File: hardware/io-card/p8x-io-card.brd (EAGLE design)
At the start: 160 x 100 mm, 36 parts, among them J1 DIN41612-96M, J2 SERIAL, SW1 INPUT, U1 IO PAGE, U10 LED PORT, U11 MON A-LO, U12 MON A-HI, U13 MON D, U14 ACIA, U15 74HCT00, U2 PORT DEC, U3 DOE DEC, U4 DLD DEC, U5 74HCT32, U6 74HCT08, U7 BAUD DIV, U8 RS232, U9 SW IN, X2 2.4576MHZ

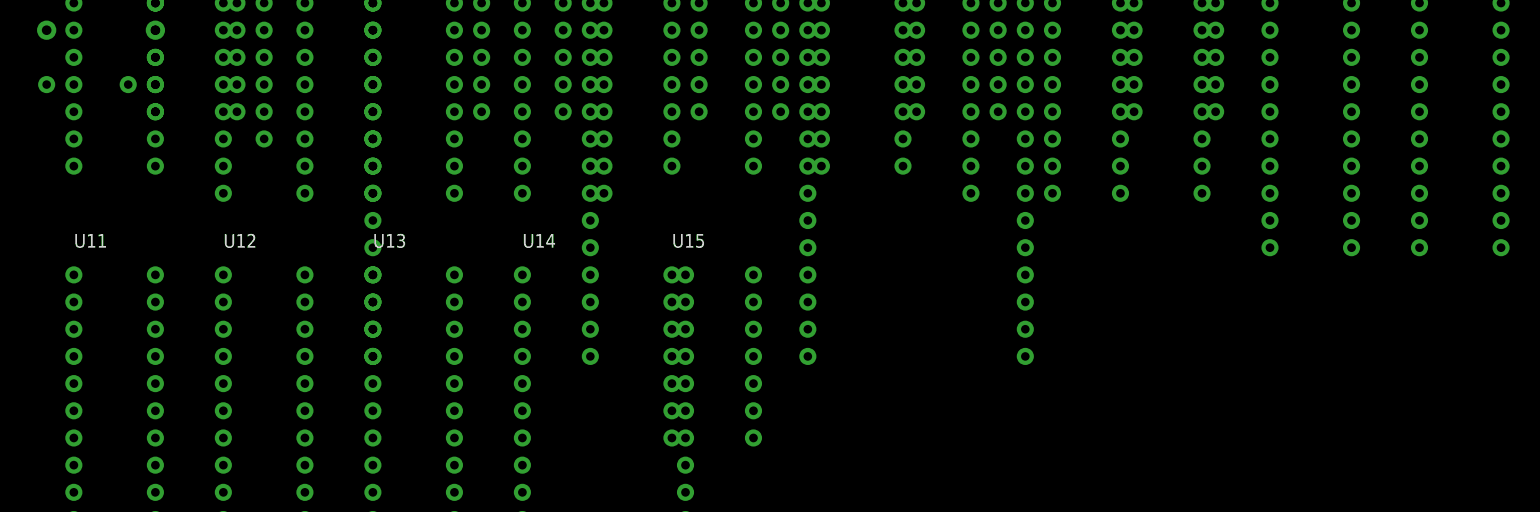
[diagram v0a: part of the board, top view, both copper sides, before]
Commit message: hw: per-IC 100nF decoupling caps on every card
card standards sec.5 requires a decoupling cap per IC; only the backplane had
them. gen_eagle's card() now generates one 100nF cap (CDn, C_DISC footprint)
per IC on the five plug-in cards, placed next to its IC and wired VCC<->GND;
the memory card's separate build does the same for U1-U9.

Caps added: control 18, regbank 44, alu 31, io 15, cf 8, memory 9. All 7
boards regenerate with 0 validation errors; card schematic PDFs refreshed.
Placement is approximate (caps sit just below each IC) pending Fusion routing.

Clears a pre-fab blocker from the backlog.

Co-Authored-By: Claude Opus 4.8 <noreply@anthropic.com>
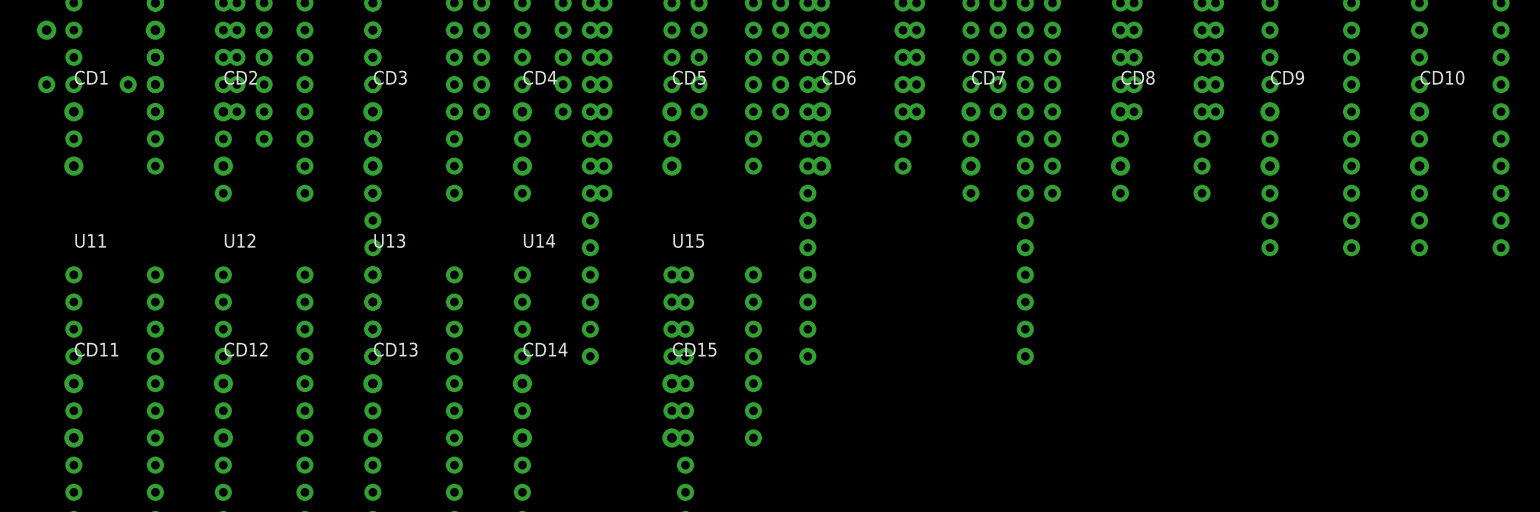
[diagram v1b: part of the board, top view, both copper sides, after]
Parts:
- added CD1, CD10, CD11, CD12, CD13, CD14, CD15, CD2, CD3, CD4, CD5, CD6, CD7, CD8, CD9: 100N, p8x:C_DISC
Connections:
- net GND: now also CD1.2, CD10.2, CD11.2, CD12.2, CD13.2, CD14.2, CD15.2, CD2.2, CD3.2, CD4.2, CD5.2, CD6.2, CD7.2, CD8.2, CD9.2
- net VCC: now also CD1.1, CD10.1, CD11.1, CD12.1, CD13.1, CD14.1, CD15.1, CD2.1, CD3.1, CD4.1, CD5.1, CD6.1, CD7.1, CD8.1, CD9.1
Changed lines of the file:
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@@
 <element name="J1" library="p8x" package="DIN96" value="DIN41612-96M" x="147.32" y="88.90"/>
 <element name="U1" library="p8x" package="DIP14" value="IO PAGE" x="7.62" y="88.90"/>
+<element name="CD1" library="p8x" package="C_DISC" value="100N" x="7.62" y="78.74"/>
 <element name="U2" library="p8x" package="DIP16" value="PORT DEC" x="21.59" y="88.90"/>
+<element name="CD2" library="p8x" package="C_DISC" value="100N" x="21.59" y="78.74"/>
 <element name="U3" library="p8x" package="DIP16" value="DOE DEC" x="35.56" y="88.90"/>
+<element name="CD3" library="p8x" package="C_DISC" value="100N" x="35.56" y="78.74"/>
 <element name="U4" library="p8x" package="DIP16" value="DLD DEC" x="49.53" y="88.90"/>
+<element name="CD4" library="p8x" package="C_DISC" value="100N" x="49.53" y="78.74"/>
 <element name="U5" library="p8x" package="DIP14" value="74HCT32" x="63.50" y="88.90"/>
+<element name="CD5" library="p8x" package="C_DISC" value="100N" x="63.50" y="78.74"/>
 <element name="U6" library="p8x" package="DIP14" value="74HCT08" x="77.47" y="88.90"/>
+<element name="CD6" library="p8x" package="C_DISC" value="100N" x="77.47" y="78.74"/>
 <element name="U7" library="p8x" package="DIP16" value="BAUD DIV" x="91.44" y="88.90"/>
+<element name="CD7" library="p8x" package="C_DISC" value="100N" x="91.44" y="78.74"/>
 <element name="U8" library="p8x" package="DIP16" value="RS232" x="105.41" y="88.90"/>
+<element name="CD8" library="p8x" package="C_DISC" value="100N" x="105.41" y="78.74"/>
 <element name="U9" library="p8x" package="DIP20" value="SW IN" x="119.38" y="88.90"/>
+<element name="CD9" library="p8x" package="C_DISC" value="100N" x="119.38" y="78.74"/>
 <element name="U10" library="p8x" package="DIP20" value="LED PORT" x="133.35" y="88.90"/>
+<element name="CD10" library="p8x" package="C_DISC" value="100N" x="133.35" y="78.74"/>
 <element name="U11" library="p8x" package="DIP20" value="MON A-LO" x="7.62" y="63.50"/>
+<element name="CD11" library="p8x" package="C_DISC" value="100N" x="7.62" y="53.34"/>
 <element name="U12" library="p8x" package="DIP20" value="MON A-HI" x="21.59" y="63.50"/>
+<element name="CD12" library="p8x" package="C_DISC" value="100N" x="21.59" y="53.34"/>
 <element name="U13" library="p8x" package="DIP20" value="MON D" x="35.56" y="63.50"/>
+<element name="CD13" library="p8x" package="C_DISC" value="100N" x="35.56" y="53.34"/>
 <element name="U14" library="p8x" package="DIP24W" value="ACIA" x="49.53" y="63.50"/>
+<element name="CD14" library="p8x" package="C_DISC" value="100N" x="49.53" y="53.34"/>
 <element name="U15" library="p8x" package="DIP14" value="74HCT00" x="63.50" y="63.50"/>
+<element name="CD15" library="p8x" package="C_DISC" value="100N" x="63.50" y="53.34"/>
 <element name="X2" library="p8x" package="OSC4" value="2.4576MHZ" x="5.08" y="96.52"/>
 <element name="SW1" library="p8x" package="DIP16" value="INPUT" x="15.24" y="96.52"/>
@@
 <contactref element="J1" pad="C31"/>
 <contactref element="J1" pad="C32"/>
+<contactref element="CD1" pad="2"/>
+<contactref element="CD2" pad="2"/>
+<contactref element="CD3" pad="2"/>
+<contactref element="CD4" pad="2"/>
+<contactref element="CD5" pad="2"/>
+<contactref element="CD6" pad="2"/>
+<contactref element="CD7" pad="2"/>
+<contactref element="CD8" pad="2"/>
+<contactref element="CD9" pad="2"/>
+<contactref element="CD10" pad="2"/>
+<contactref element="CD11" pad="2"/>
+<contactref element="CD12" pad="2"/>
+<contactref element="CD13" pad="2"/>
+<contactref element="CD14" pad="2"/>
+<contactref element="CD15" pad="2"/>
 <polygon width="0.254" layer="2" isolate="0.3" rank="1">
 <vertex x="0" y="0"/>
@@
 <contactref element="J1" pad="C1"/>
 <contactref element="J1" pad="C2"/>
+<contactref element="CD1" pad="1"/>
+<contactref element="CD2" pad="1"/>
+<contactref element="CD3" pad="1"/>
+<contactref element="CD4" pad="1"/>
+<contactref element="CD5" pad="1"/>
+<contactref element="CD6" pad="1"/>
+<contactref element="CD7" pad="1"/>
+<contactref element="CD8" pad="1"/>
+<contactref element="CD9" pad="1"/>
+<contactref element="CD10" pad="1"/>
+<contactref element="CD11" pad="1"/>
+<contactref element="CD12" pad="1"/>
+<contactref element="CD13" pad="1"/>
+<contactref element="CD14" pad="1"/>
+<contactref element="CD15" pad="1"/>
 <polygon width="0.254" layer="15" isolate="0.3" rank="1">
 <vertex x="0" y="0"/>

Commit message: feat(hw): provision RTC + CF 8-bit fallback footprints (rev C, DNP)
The last two pre-fab board items, both Do-Not-Populate so the options exist
post-fab without a respin.

- I/O card: DS1302 RTC (U16) + 32.768kHz crystal (X3) + backup coin cell (BT1)
  + a 3-wire breakout header (J3). Fully isolated peripheral (crystal across
  X1/X2, VCC1 from +5, VCC2 from the cell, CE/SCLK/IO to J3) — no bus contention
  possible. Reserved I/O address $FF08 (PORT DEC U2 Y3). Crystal + coin-cell use
  placeholder THT footprints; VERIFY land patterns against real parts before fab.
- CF card: 8-bit fallback latch (U9, 74374). CF high data byte D8-15 wired to its
  inputs; output forced high-Z and clock grounded (inert). Populate + wire the
  bus output + decode only if a CF card refuses 8-bit mode (drives the data bus,
  so design with DRC).
- New device defs DS1302/XTAL32/COIN + a DIP8 package.

All 7 boards regenerate with 0 validation errors; all 6 test suites pass.

Co-Authored-By: Claude Opus 4.8 <noreply@anthropic.com>
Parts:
- added BT1: CR2032, p8x:CP_RADIAL
- added CD16: 100N, p8x:C_DISC
- added J3: RTC 3-WIRE, p8x:HDR3
- added U16: RTC DNP, p8x:DIP8
- added X3: 32.768KHZ, p8x:C_DISC
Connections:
- new net RTCCE: J3.1, U16.5
- new net RTCIO: J3.3, U16.6
- new net RTCSCLK: J3.2, U16.7
- new net RTCX1: U16.2, X3.1
- new net RTCX2: U16.3, X3.2
- new net VBAT: BT1.1, U16.1
- net GND: now also BT1.2, CD16.2, U16.4
- net VCC: now also CD16.1, U16.8
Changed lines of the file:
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@@
 <element name="U15" library="p8x" package="DIP14" value="74HCT00" x="63.50" y="63.50"/>
 <element name="CD15" library="p8x" package="C_DISC" value="100N" x="63.50" y="53.34"/>
+<element name="U16" library="p8x" package="DIP8" value="RTC DNP" x="77.47" y="63.50"/>
+<element name="CD16" library="p8x" package="C_DISC" value="100N" x="77.47" y="53.34"/>
 <element name="X2" library="p8x" package="OSC4" value="2.4576MHZ" x="5.08" y="96.52"/>
 <element name="SW1" library="p8x" package="DIP16" value="INPUT" x="15.24" y="96.52"/>
@@
 <element name="R4" library="p8x" package="R_AXIAL" value="1K" x="45.72" y="91.44"/>
 <element name="LED4" library="p8x" package="LED5" value="IOSEL-YEL" x="55.88" y="91.44"/>
+<element name="X3" library="p8x" package="C_DISC" value="32.768KHZ" x="66.04" y="91.44"/>
+<element name="BT1" library="p8x" package="CP_RADIAL" value="CR2032" x="76.20" y="91.44"/>
+<element name="J3" library="p8x" package="HDR3" value="RTC 3-WIRE" x="86.36" y="91.44"/>
 </elements><signals>
 <signal name="-MEMW">
@@
 <contactref element="U6" pad="1"/>
 <contactref element="U6" pad="2"/>
+<contactref element="U16" pad="4"/>
+<contactref element="BT1" pad="2"/>
 <contactref element="J1" pad="A31"/>
 <contactref element="J1" pad="A32"/>
@@
 <contactref element="CD14" pad="2"/>
 <contactref element="CD15" pad="2"/>
+<contactref element="CD16" pad="2"/>
 <polygon width="0.254" layer="2" isolate="0.3" rank="1">
 <vertex x="0" y="0"/>
@@
 <contactref element="U6" pad="4"/>
 </signal>
+<signal name="RTCCE">
+<contactref element="U16" pad="5"/>
+<contactref element="J3" pad="1"/>
+</signal>
+<signal name="RTCIO">
+<contactref element="U16" pad="6"/>
+<contactref element="J3" pad="3"/>
+</signal>
+<signal name="RTCSCLK">
+<contactref element="U16" pad="7"/>
+<contactref element="J3" pad="2"/>
+</signal>
+<signal name="RTCX1">
+<contactref element="U16" pad="2"/>
+<contactref element="X3" pad="1"/>
+</signal>
+<signal name="RTCX2">
+<contactref element="U16" pad="3"/>
+<contactref element="X3" pad="2"/>
+</signal>
 <signal name="RXD">
 <contactref element="U14" pad="2"/>
@@
 <contactref element="U14" pad="6"/>
 <contactref element="U8" pad="11"/>
+</signal>
+<signal name="VBAT">
+<contactref element="U16" pad="1"/>
+<contactref element="BT1" pad="1"/>
 </signal>
 <signal name="VCC">
@@
 <contactref element="U7" pad="1"/>
 <contactref element="RP1" pad="1"/>
+<contactref element="U16" pad="8"/>
 <contactref element="J1" pad="A1"/>
 <contactref element="J1" pad="A2"/>
@@
 <contactref element="CD14" pad="1"/>
 <contactref element="CD15" pad="1"/>
+<contactref element="CD16" pad="1"/>
 <polygon width="0.254" layer="15" isolate="0.3" rank="1">
 <vertex x="0" y="0"/>
